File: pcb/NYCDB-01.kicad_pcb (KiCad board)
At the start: 2 copper layers, 263 parts, among them J1 AUDIO_JACK, J2 AUDIO_JACK, P1 CONN_BATT, P2 USB_OTG, Q1 Q_PMOS_GSD, SW1 SW_POWER, SW2 SW_RESET, U1 CS5361, U10 OPA4134, U11 TPA6120A2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

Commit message: Working on the switcher now
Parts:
- moved D9 12.8 mm to (119.4, 33.0), turned to 180 degrees
- moved Q1 11.5 mm to (114.3, 33.0)
- moved R101 9.67 mm to (175.3, 66.0)
- moved R103 9.67 mm to (189.2, 66.0)
- moved C104 9.67 mm to (147.3, 61.0)
- moved C105 9.67 mm to (161.3, 61.0)
- moved C100 9.67 mm to (175.3, 62.2)
- moved C101 9.67 mm to (189.2, 62.2)
- moved R100 9.67 mm to (180.3, 66.0)
- moved R102 9.67 mm to (194.3, 66.0)
- moved C102 9.67 mm to (152.4, 61.0)
- moved C103 9.67 mm to (166.4, 61.0)
- moved C106 9.67 mm to (180.3, 62.2)
- moved C107 9.67 mm to (194.3, 62.2)
- moved U15 9.67 mm to (148.6, 57.1)
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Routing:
- net -15V: track 25.8 -> 107.4 mm
- net +3V3: track 424.0 -> 363.3 mm
- net +15V: track 17.0 -> 70.5 mm
- net Net-(R96-Pad2): track 0.00 -> 38.2 mm, vias 0 -> 2
- net Net-(Q1-Pad1): track 1.64 -> 36.4 mm, vias 1 -> 0
- net +5V: track 226.7 -> 197.9 mm
- net /Power Supplies/V_BATT: track 211.0 -> 197.8 mm, vias 2 -> 4
- net /Power Supplies/PWR_SW: track 67.0 -> 57.5 mm, vias 2 -> 4
- net +1V2: track 105.8 -> 100.6 mm
- net Net-(D9-Pad2): track 0.00 -> 5.07 mm
- net Net-(D9-Pad1): track 0.00 -> 4.11 mm
- net Net-(C35-Pad2): track 45.6 -> 42.0 mm
- net Net-(C32-Pad2): track 55.3 -> 51.8 mm
- net GND: track 196.0 -> 197.5 mm, vias 126 -> 127
- net Net-(R42-Pad2): track 72.7 -> 71.8 mm
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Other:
- board text added: "FAULT"

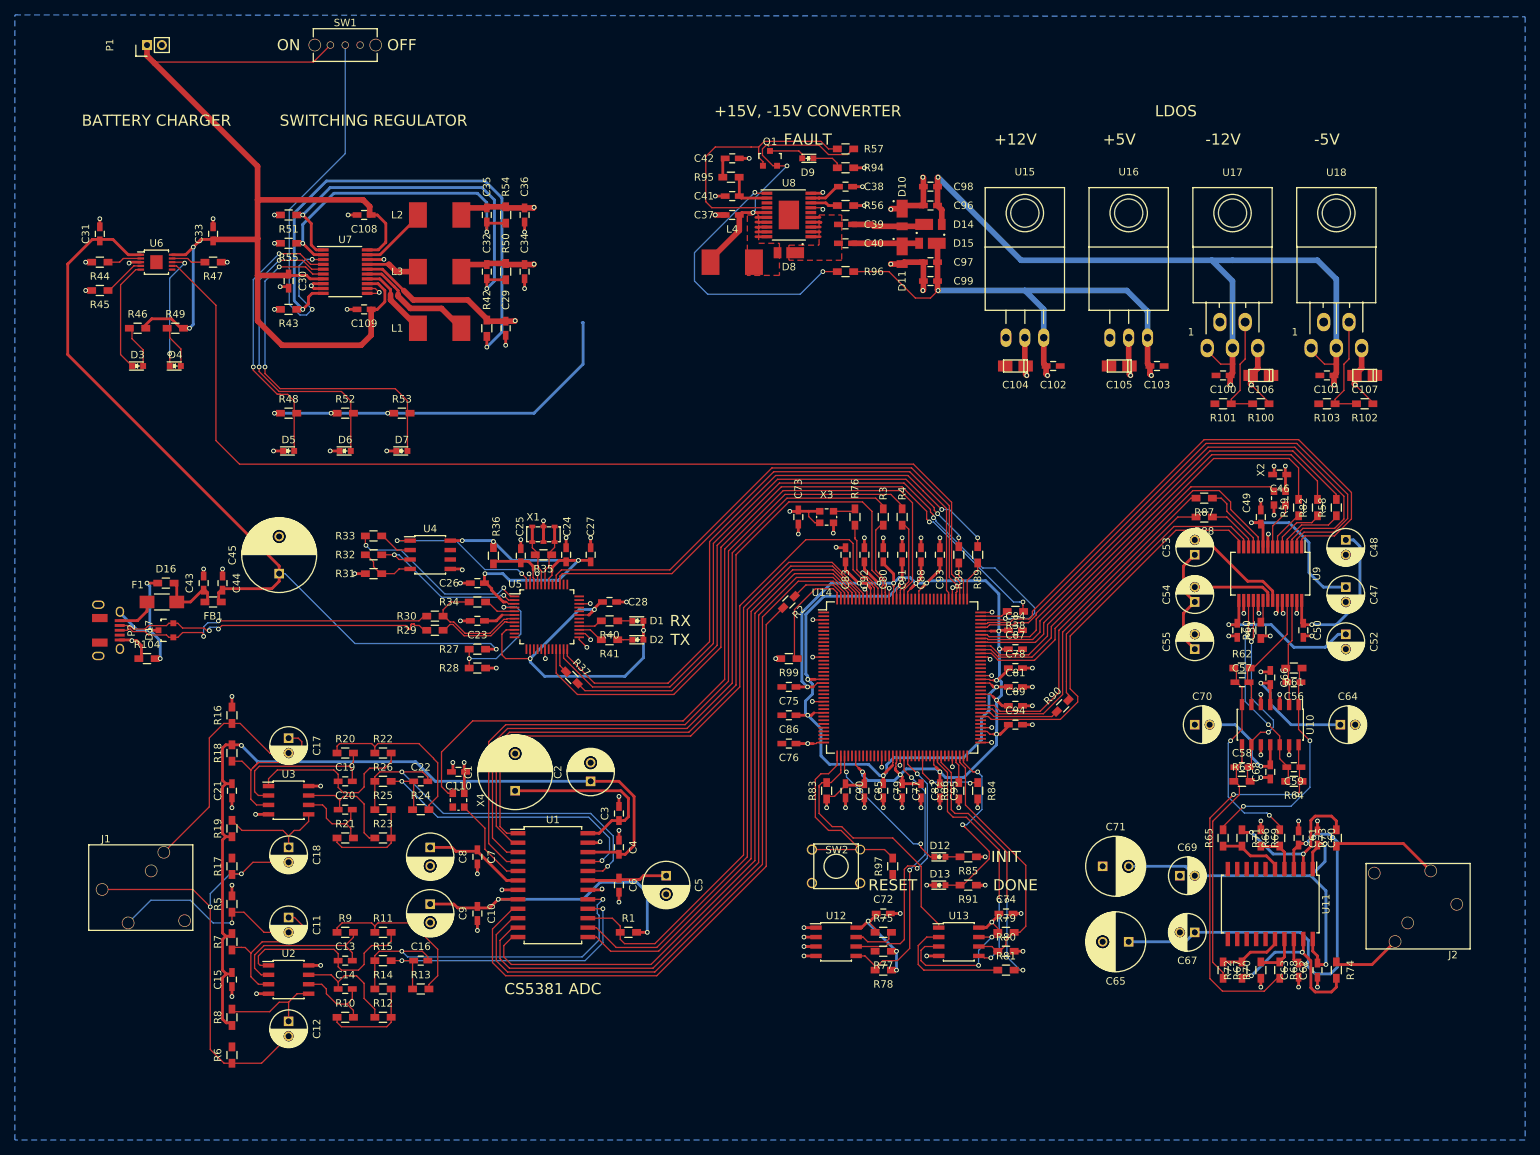
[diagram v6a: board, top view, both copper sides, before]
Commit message: Cleaned up the rest of the power blocks
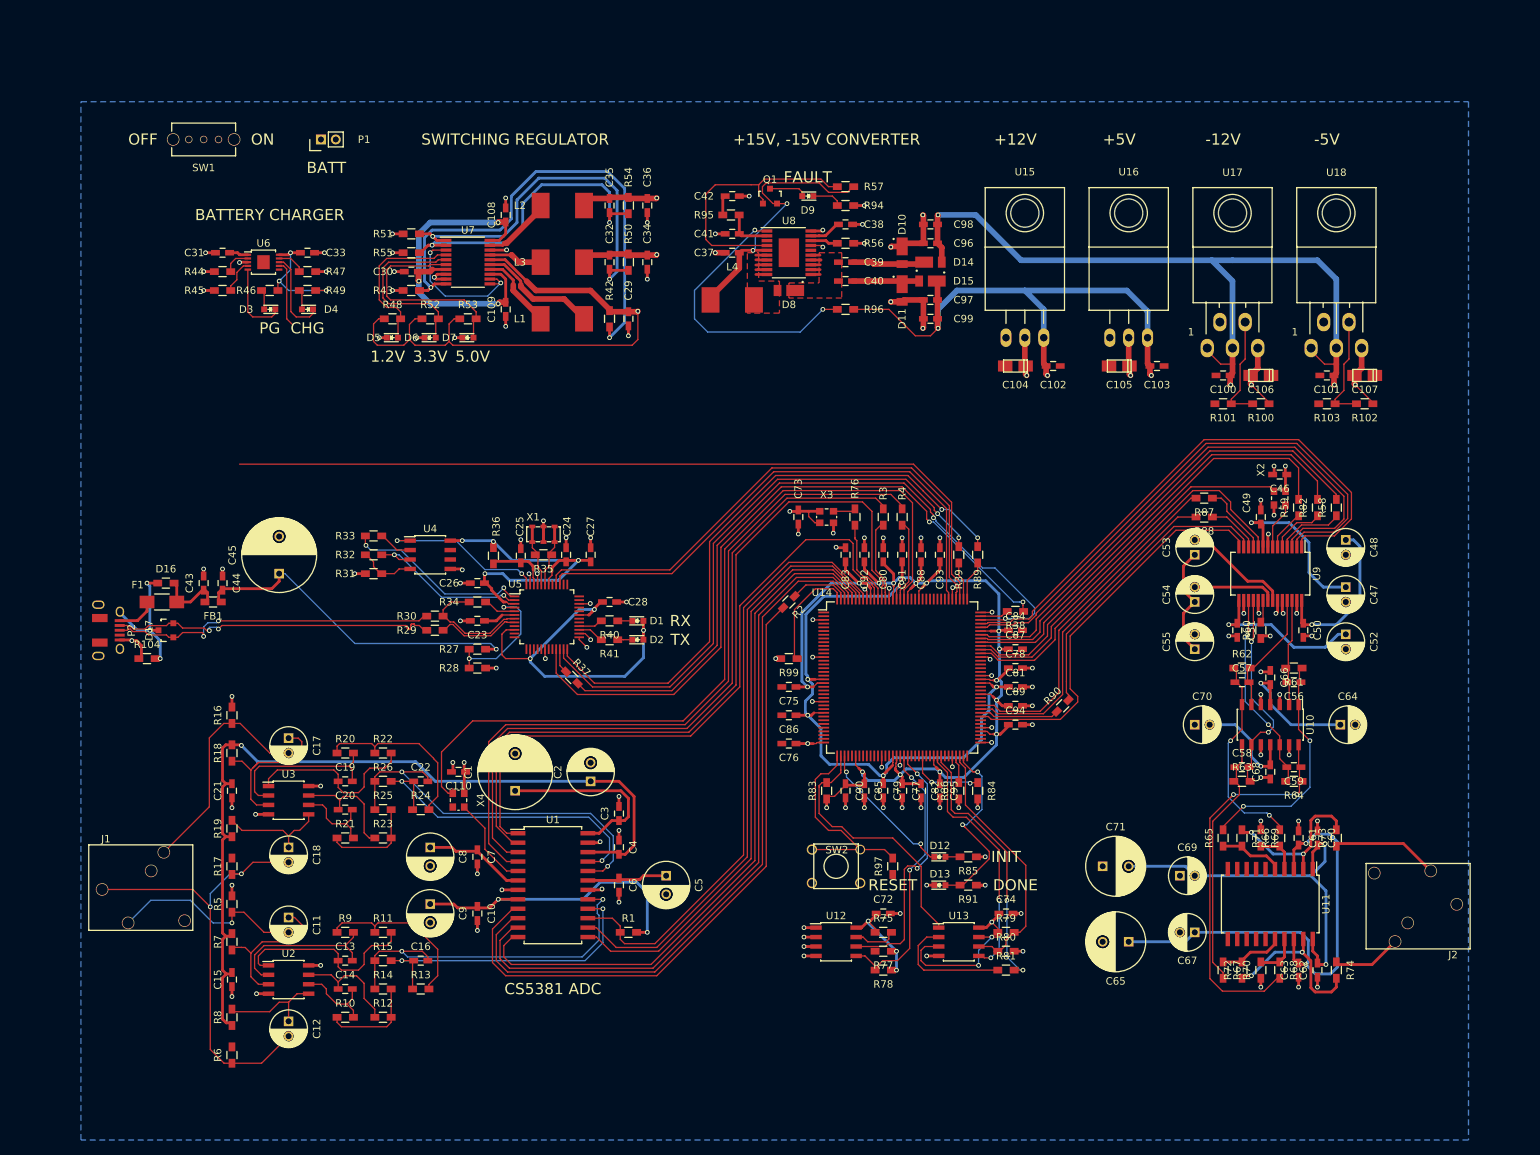
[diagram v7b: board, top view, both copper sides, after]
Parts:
- moved P1 26.6 mm to (53.9, 30.5)
- moved SW1 22.9 mm to (38.1, 30.5), turned to 180 degrees
- moved D5 20.7 mm to (63.5, 57.1)
- moved D3 19.3 mm to (47.0, 53.3), turned to 180 degrees
- moved D4 19.3 mm to (52.1, 53.3), turned to 180 degrees
- moved D6 19.1 mm to (68.6, 57.1)
- moved C108 19.0 mm to (78.7, 40.6), turned to 90 degrees
- moved C109 19.0 mm to (78.7, 53.3), turned to 270 degrees
- moved R48 18.9 mm to (63.5, 54.6)
- moved R46 18.5 mm to (47.0, 50.8)
- moved R49 18.5 mm to (52.1, 50.8)
- moved D7 17.6 mm to (73.7, 57.1)
- moved R52 17.1 mm to (68.6, 54.6)
- moved R43 16.7 mm to (66.0, 50.8)
- moved R51 16.7 mm to (66.0, 43.2)
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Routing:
- net /Power Supplies/V_BATT: track 197.8 -> 102.4 mm, vias 4 -> 8
- net /FT2232D/USB5V: track 111.4 -> 48.5 mm
- net /Power Supplies/PWR_SW: track 57.5 -> 22.1 mm, vias 4 -> 3
- net /Power Supplies/ISET2: track 142.2 -> 120.4 mm
- net Net-(D7-Pad2): track 48.9 -> 28.3 mm, vias 2 -> 0
- net Net-(D6-Pad2): track 43.2 -> 24.8 mm, vias 2 -> 0
- net Net-(D5-Pad2): track 37.9 -> 21.3 mm, vias 2 -> 0
- net Net-(R42-Pad2): track 71.8 -> 66.7 mm
- net Net-(D4-Pad1): track 16.4 -> 11.7 mm, vias 2 -> 0
- net Net-(D3-Pad1): track 15.1 -> 10.4 mm
- net +15V: track 70.5 -> 74.1 mm
- net Net-(D3-Pad2): track 5.70 -> 2.69 mm
- net Net-(D4-Pad2): track 5.70 -> 2.69 mm
- net -15V: track 107.4 -> 105.2 mm
- net Net-(R45-Pad1): track 6.14 -> 4.61 mm
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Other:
- board text added: "1.2V"
- board text added: "3.3V"
- board text added: "5.0V"
- board text added: "BATT"
- board text added: "CHG"
- board text added: "PG"
- board text removed: "LDOS"

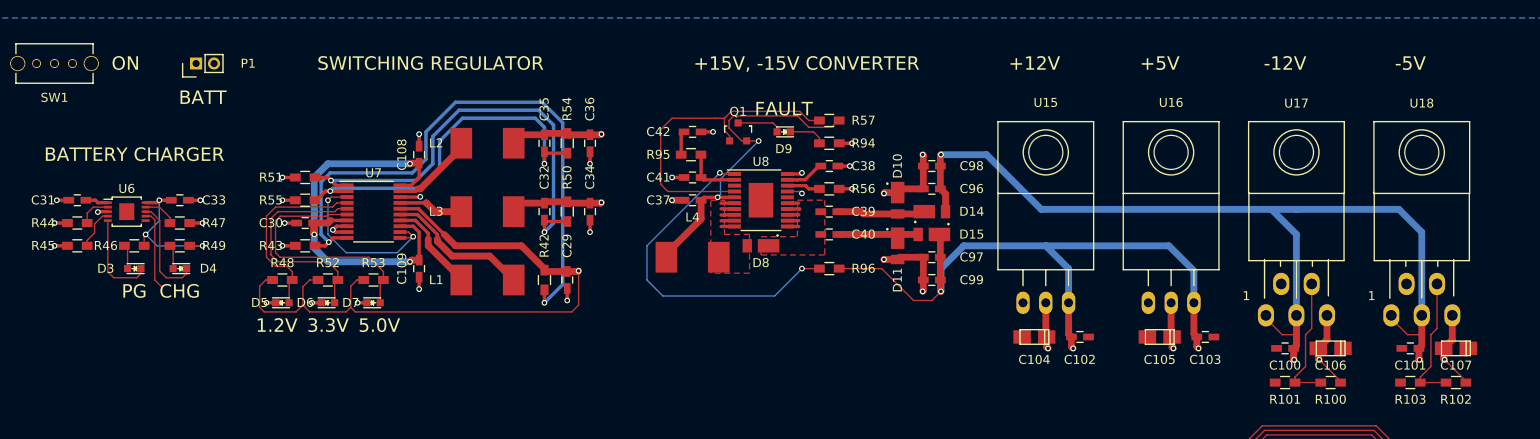
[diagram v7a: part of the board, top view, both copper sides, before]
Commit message: Finished cleaning up and connecting most of the power logic
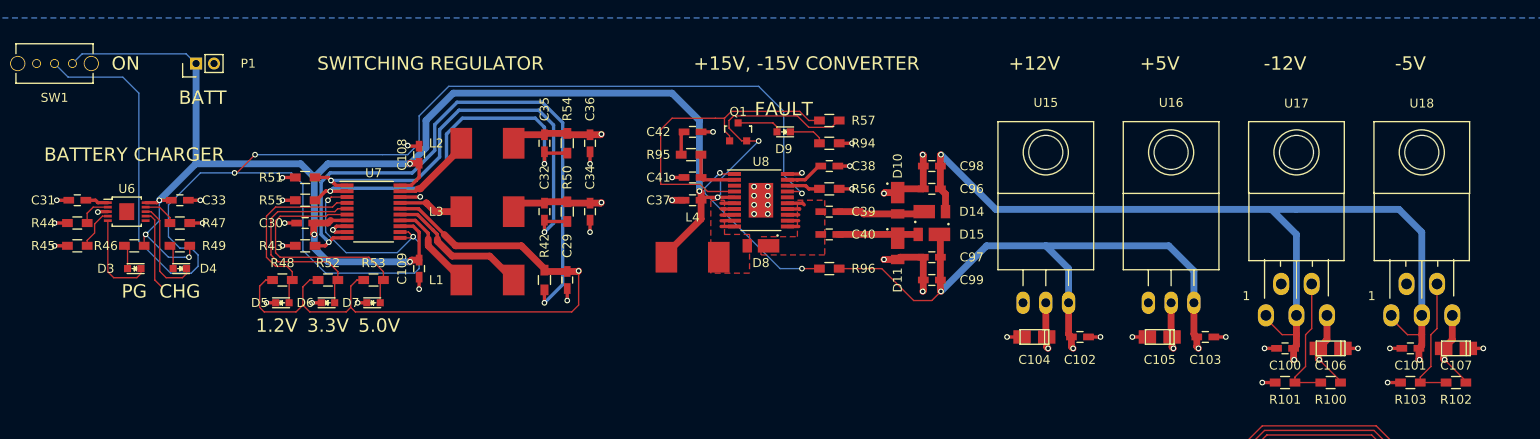
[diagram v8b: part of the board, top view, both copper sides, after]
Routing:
- net /Power Supplies/PWR_SW: track 22.1 -> 187.5 mm, vias 3 -> 5
- net /Power Supplies/V_BATT: track 102.4 -> 194.2 mm, vias 8 -> 9
- net Net-(R96-Pad2): track 38.2 -> 20.9 mm
- net GND: track 198.1 -> 213.0 mm, vias 127 -> 145
- net +15V: track 74.1 -> 72.7 mm
- net Net-(C39-Pad2): track 6.38 -> 7.10 mm
